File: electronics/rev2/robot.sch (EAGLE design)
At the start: 77 parts, among them J1 USB-B, J2 DC21MMX, J3 B6B-ZR, J4 B6B-ZR, J5 B6B-ZR, J6 KICKER, Q1 IRLMS2002TRPBF, Q2 IRLMS2002TRPBF, Q3 NPN_BC817,215, Q4 SUD50N04-8M8P-4GE3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

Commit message: Re-camming, minor renamings
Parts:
- renumbered U$1 to SW1, U$12 to U11, U$13 to U12, U$25 to U8, U$7 to U10
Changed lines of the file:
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@@
 <attribute name="VALUE" value="0.3"/>
 </part>
-<part name="U$25" library="rhoban" deviceset="TS2940CW-3.3RP" device="">
+<part name="U8" library="rhoban" deviceset="TS2940CW-3.3RP" device="">
 <attribute name="FARNELL" value="7261403"/>
 </part>
@@
 <attribute name="VALUE" value="0.33µF"/>
 </part>
-<part name="U$1" library="rhoban" deviceset="L102011ML04Q" device=""/>
-<part name="U$7" library="rhoban" deviceset="TB67H450FNG" device=""/>
+<part name="SW1" library="rhoban" deviceset="L102011ML04Q" device=""/>
+<part name="U10" library="rhoban" deviceset="TB67H450FNG" device=""/>
 <part name="R19" library="rcl" deviceset="R-EU_" device="R1206" value="0.33"/>
-<part name="U$12" library="rhoban" deviceset="TB67H450FNG" device=""/>
+<part name="U11" library="rhoban" deviceset="TB67H450FNG" device=""/>
 <part name="R20" library="rcl" deviceset="R-EU_" device="R1206" value="0.33"/>
-<part name="U$13" library="rhoban" deviceset="TB67H450FNG" device=""/>
+<part name="U12" library="rhoban" deviceset="TB67H450FNG" device=""/>
 <part name="R21" library="rcl" deviceset="R-EU_" device="R1206" value="0.33"/>
 <part name="GND2" library="supply1" deviceset="GND" device=""/>
@@
 <attribute name="FARNELL" x="-2.54" y="38.1" size="1.778" layer="96" display="off"/>
 </instance>
-<instance part="U$25" gate="G$1" x="71.12" y="-25.4">
+<instance part="U8" gate="G$1" x="71.12" y="-25.4">
 <attribute name="FARNELL" x="71.12" y="-25.4" size="1.778" layer="96" display="off"/>
 </instance>
@@
 <attribute name="FARNELL" x="7.62" y="7.62" size="1.778" layer="96" display="off"/>
 </instance>
-<instance part="U$1" gate="G$1" x="-50.8" y="38.1"/>
+<instance part="SW1" gate="G$1" x="-50.8" y="38.1"/>
 </instances>
 <busses>
@@
 </segment>
 <segment>
-<pinref part="U$25" gate="G$1" pin="GND"/>
+<pinref part="U8" gate="G$1" pin="GND"/>
 <wire x1="71.12" y1="-33.02" x2="71.12" y2="-38.1" width="0.1524" layer="91"/>
 <label x="71.12" y="-38.1" size="1.27" layer="95" xref="yes"/>
@@
 <junction x="-20.32" y="35.56"/>
 <wire x1="-30.48" y1="35.56" x2="-30.48" y2="43.18" width="0.1524" layer="91"/>
-<pinref part="U$1" gate="G$1" pin="A"/>
+<pinref part="SW1" gate="G$1" pin="A"/>
 <wire x1="-30.48" y1="43.18" x2="-33.02" y2="43.18" width="0.1524" layer="91"/>
 </segment>
@@
 </segment>
 <segment>
-<pinref part="U$25" gate="G$1" pin="IN"/>
+<pinref part="U8" gate="G$1" pin="IN"/>
 <wire x1="60.96" y1="-25.4" x2="50.8" y2="-25.4" width="0.1524" layer="91"/>
 <label x="50.8" y="-25.4" size="1.27" layer="95" rot="R90" xref="yes"/>
@@
 <pinref part="J2" gate="G$1" pin="2"/>
 <wire x1="-66.04" y1="38.1" x2="-73.66" y2="38.1" width="0.1524" layer="91"/>
-<pinref part="U$1" gate="G$1" pin="COM"/>
+<pinref part="SW1" gate="G$1" pin="COM"/>
 </segment>
 </net>
@@
 </segment>
 <segment>
-<pinref part="U$25" gate="G$1" pin="OUT"/>
+<pinref part="U8" gate="G$1" pin="OUT"/>
 <wire x1="81.28" y1="-25.4" x2="93.98" y2="-25.4" width="0.1524" layer="91"/>
 <label x="93.98" y="-25.4" size="1.27" layer="95" rot="R90" xref="yes"/>
@@
 <attribute name="FARNELL" x="-60.96" y="-27.94" size="1.778" layer="96" display="off"/>
 </instance>
-<instance part="U$7" gate="G$1" x="-15.24" y="25.4"/>
+<instance part="U10" gate="G$1" x="-15.24" y="25.4"/>
 <instance part="R19" gate="G$1" x="7.62" y="27.94"/>
-<instance part="U$12" gate="G$1" x="-15.24" y="-2.54"/>
+<instance part="U11" gate="G$1" x="-15.24" y="-2.54"/>
 <instance part="R20" gate="G$1" x="7.62" y="0"/>
-<instance part="U$13" gate="G$1" x="-15.24" y="-30.48"/>
+<instance part="U12" gate="G$1" x="-15.24" y="-30.48"/>
 <instance part="R21" gate="G$1" x="7.62" y="-27.94"/>
 <instance part="GND2" gate="1" x="-76.2" y="17.78"/>
@@
 </segment>
 <segment>
-<pinref part="U$7" gate="G$1" pin="GND"/>
+<pinref part="U10" gate="G$1" pin="GND"/>
 <wire x1="-33.02" y1="33.02" x2="-38.1" y2="33.02" width="0.1524" layer="91"/>
 <label x="-38.1" y="33.02" size="1.27" layer="95" rot="R180" xref="yes"/>
@@
 </segment>
 <segment>
-<pinref part="U$12" gate="G$1" pin="GND"/>
+<pinref part="U11" gate="G$1" pin="GND"/>
 <wire x1="-33.02" y1="5.08" x2="-38.1" y2="5.08" width="0.1524" layer="91"/>
 <label x="-38.1" y="5.08" size="1.27" layer="95" rot="R180" xref="yes"/>
@@
 </segment>
 <segment>
-<pinref part="U$13" gate="G$1" pin="GND"/>
+<pinref part="U12" gate="G$1" pin="GND"/>
 <wire x1="-33.02" y1="-22.86" x2="-38.1" y2="-22.86" width="0.1524" layer="91"/>
 <label x="-38.1" y="-22.86" size="1.27" layer="95" rot="R180" xref="yes"/>
@@
 <net name="M1A" class="0">
 <segment>
-<pinref part="U$7" gate="G$1" pin="IN1"/>
+<pinref part="U10" gate="G$1" pin="IN1"/>
 <wire x1="-33.02" y1="22.86" x2="-38.1" y2="22.86" width="0.1524" layer="91"/>
 <label x="-38.1" y="22.86" size="1.27" layer="95" rot="R180" xref="yes"/>
@@
 <net name="M1B" class="0">
 <segment>
-<pinref part="U$7" gate="G$1" pin="IN2"/>
+<pinref part="U10" gate="G$1" pin="IN2"/>
 <wire x1="-33.02" y1="27.94" x2="-38.1" y2="27.94" width="0.1524" layer="91"/>
 <label x="-38.1" y="27.94" size="1.27" layer="95" rot="R180" xref="yes"/>
@@
 </segment>
 <segment>
-<pinref part="U$12" gate="G$1" pin="OUT2"/>
+<pinref part="U11" gate="G$1" pin="OUT2"/>
 <wire x1="0" y1="5.08" x2="5.08" y2="5.08" width="0.1524" layer="91"/>
 <label x="5.08" y="5.08" size="1.27" layer="95" xref="yes"/>
@@
 <net name="M2A" class="0">
 <segment>
-<pinref part="U$12" gate="G$1" pin="IN1"/>
+<pinref part="U11" gate="G$1" pin="IN1"/>
 <wire x1="-33.02" y1="-5.08" x2="-38.1" y2="-5.08" width="0.1524" layer="91"/>
 <label x="-38.1" y="-5.08" size="1.27" layer="95" rot="R180" xref="yes"/>
@@
 <net name="M2B" class="0">
 <segment>
-<pinref part="U$12" gate="G$1" pin="IN2"/>
+<pinref part="U11" gate="G$1" pin="IN2"/>
 <wire x1="-33.02" y1="0" x2="-38.1" y2="0" width="0.1524" layer="91"/>
 <label x="-38.1" y="0" size="1.27" layer="95" rot="R180" xref="yes"/>
@@
 <net name="M3A" class="0">
 <segment>
-<pinref part="U$13" gate="G$1" pin="IN1"/>
+<pinref part="U12" gate="G$1" pin="IN1"/>
 <wire x1="-33.02" y1="-33.02" x2="-38.1" y2="-33.02" width="0.1524" layer="91"/>
 <label x="-38.1" y="-33.02" size="1.27" layer="95" rot="R180" xref="yes"/>
@@
 <net name="M3B" class="0">
 <segment>
-<pinref part="U$13" gate="G$1" pin="IN2"/>
+<pinref part="U12" gate="G$1" pin="IN2"/>
 <wire x1="-33.02" y1="-27.94" x2="-38.1" y2="-27.94" width="0.1524" layer="91"/>
 <label x="-38.1" y="-27.94" size="1.27" layer="95" rot="R180" xref="yes"/>
@@
 </segment>
 <segment>
-<pinref part="U$7" gate="G$1" pin="OUT1"/>
+<pinref part="U10" gate="G$1" pin="OUT1"/>
 <wire x1="0" y1="22.86" x2="5.08" y2="22.86" width="0.1524" layer="91"/>
 <label x="5.08" y="22.86" size="1.27" layer="95" xref="yes"/>
@@
 </segment>
 <segment>
-<pinref part="U$7" gate="G$1" pin="OUT2"/>
+<pinref part="U10" gate="G$1" pin="OUT2"/>
 <wire x1="0" y1="33.02" x2="5.08" y2="33.02" width="0.1524" layer="91"/>
 <label x="5.08" y="33.02" size="1.27" layer="95" xref="yes"/>
@@
 </segment>
 <segment>
-<pinref part="U$12" gate="G$1" pin="OUT1"/>
+<pinref part="U11" gate="G$1" pin="OUT1"/>
 <wire x1="0" y1="-5.08" x2="5.08" y2="-5.08" width="0.1524" layer="91"/>
 <label x="5.08" y="-5.08" size="1.27" layer="95" xref="yes"/>
@@
 </segment>
 <segment>
-<pinref part="U$13" gate="G$1" pin="OUT2"/>
+<pinref part="U12" gate="G$1" pin="OUT2"/>
 <wire x1="0" y1="-22.86" x2="5.08" y2="-22.86" width="0.1524" layer="91"/>
 <label x="5.08" y="-22.86" size="1.27" layer="95" xref="yes"/>
@@
 </segment>
 <segment>
-<pinref part="U$13" gate="G$1" pin="OUT1"/>
+<pinref part="U12" gate="G$1" pin="OUT1"/>
 <wire x1="0" y1="-33.02" x2="5.08" y2="-33.02" width="0.1524" layer="91"/>
 <label x="5.08" y="-33.02" size="1.27" layer="95" xref="yes"/>
@@
 </segment>
 <segment>
-<pinref part="U$7" gate="G$1" pin="VM"/>
+<pinref part="U10" gate="G$1" pin="VM"/>
 <wire x1="0" y1="17.78" x2="5.08" y2="17.78" width="0.1524" layer="91"/>
 <label x="5.08" y="17.78" size="1.27" layer="95" xref="yes"/>
 </segment>
 <segment>
-<pinref part="U$12" gate="G$1" pin="VM"/>
+<pinref part="U11" gate="G$1" pin="VM"/>
 <wire x1="0" y1="-10.16" x2="5.08" y2="-10.16" width="0.1524" layer="91"/>
 <label x="5.08" y="-10.16" size="1.27" layer="95" xref="yes"/>
 </segment>
 <segment>
-<pinref part="U$13" gate="G$1" pin="VM"/>
+<pinref part="U12" gate="G$1" pin="VM"/>
 <wire x1="0" y1="-38.1" x2="5.08" y2="-38.1" width="0.1524" layer="91"/>
 <label x="5.08" y="-38.1" size="1.27" layer="95" xref="yes"/>
@@
 </segment>
 <segment>
-<pinref part="U$7" gate="G$1" pin="VREF"/>
+<pinref part="U10" gate="G$1" pin="VREF"/>
 <wire x1="-33.02" y1="17.78" x2="-38.1" y2="17.78" width="0.1524" layer="91"/>
 <label x="-38.1" y="17.78" size="1.27" layer="95" rot="R180" xref="yes"/>
 </segment>
 <segment>
-<pinref part="U$12" gate="G$1" pin="VREF"/>
+<pinref part="U11" gate="G$1" pin="VREF"/>
 <wire x1="-33.02" y1="-10.16" x2="-38.1" y2="-10.16" width="0.1524" layer="91"/>
 <label x="-38.1" y="-10.16" size="1.27" layer="95" rot="R180" xref="yes"/>
 </segment>
 <segment>
-<pinref part="U$13" gate="G$1" pin="VREF"/>
+<pinref part="U12" gate="G$1" pin="VREF"/>
 <wire x1="-33.02" y1="-38.1" x2="-38.1" y2="-38.1" width="0.1524" layer="91"/>
 <label x="-38.1" y="-38.1" size="1.27" layer="95" rot="R180" xref="yes"/>
@@
 <net name="N$18" class="1">
 <segment>
-<pinref part="U$7" gate="G$1" pin="RS"/>
+<pinref part="U10" gate="G$1" pin="RS"/>
 <pinref part="R19" gate="G$1" pin="1"/>
 <wire x1="2.54" y1="27.94" x2="0" y2="27.94" width="0.1524" layer="91"/>
@@
 <net name="N$20" class="1">
 <segment>
-<pinref part="U$12" gate="G$1" pin="RS"/>
+<pinref part="U11" gate="G$1" pin="RS"/>
 <pinref part="R20" gate="G$1" pin="1"/>
 <wire x1="2.54" y1="0" x2="0" y2="0" width="0.1524" layer="91"/>
@@
 <net name="N$21" class="1">
 <segment>
-<pinref part="U$13" gate="G$1" pin="RS"/>
+<pinref part="U12" gate="G$1" pin="RS"/>
 <pinref part="R21" gate="G$1" pin="1"/>
 <wire x1="2.54" y1="-27.94" x2="0" y2="-27.94" width="0.1524" layer="91"/>

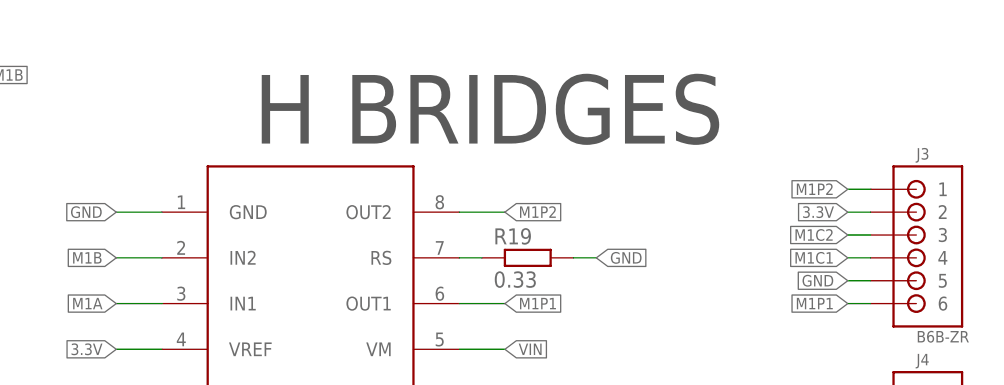
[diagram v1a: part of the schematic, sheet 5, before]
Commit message: Sheet titles
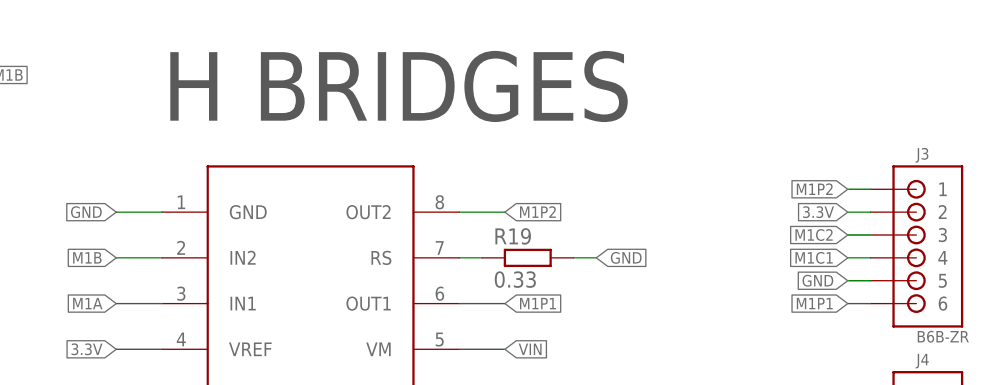
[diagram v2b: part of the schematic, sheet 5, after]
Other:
- note added: "BOOSTER (KICKER)"
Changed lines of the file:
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@@
 <sheet>
 <plain>
-<text x="-22.86" y="40.64" size="7.62" layer="97">H BRIDGES</text>
+<text x="-33.02" y="43.18" size="7.62" layer="97">H BRIDGES</text>
 <frame x1="-96.52" y1="-55.88" x2="71.12" y2="63.5" columns="8" rows="5" layer="95"/>
 </plain>
@@
 <plain>
 <frame x1="-86.36" y1="-50.8" x2="129.54" y2="43.18" columns="8" rows="5" layer="95"/>
+<text x="-27.94" y="25.4" size="7.62" layer="97">BOOSTER (KICKER)</text>
 </plain>
 <instances>

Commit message: Adding D2 diode
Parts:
- added D2: (no value), SparkFun-DiscreteSemi:DIODESOD
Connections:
- new net N$22: D2.C, Q7.D
- net N$13: now also D2.A; no longer Q7.D
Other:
- moved on the sheet: C17, Q7, R18
